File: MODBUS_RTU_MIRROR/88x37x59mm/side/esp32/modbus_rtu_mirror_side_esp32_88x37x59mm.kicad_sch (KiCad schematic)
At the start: 38 parts, among them J1 Conn_01x04_Male, J2 Conn_01x04_Male, J3 Conn_01x06_Male, SW1 SW_Push, U1 ESP32-WROOM-32, U2 TXS0108EPW, U3 AMS1117-3.3, U4 DS3231MZ, U5 FM24C64C

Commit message: created 90 degree 3mm led socket holder
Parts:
- D1: footprint LED_THT:LED_D3.0mm -> LED_THT_horizontal_holder:LED_D3.0mm_4.5x9.5mm
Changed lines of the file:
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@@
     (property "Reference" "D1" (id 0) (at 237.1725 31.75 0))
     (property "Value" "LED" (id 1) (at 237.1725 34.29 0))
-    (property "Footprint" "LED_THT:LED_D3.0mm" (id 2) (at 238.76 38.1 0)
+    (property "Footprint" "LED_THT_horizontal_holder:LED_D3.0mm_4.5x9.5mm" (id 2) (at 238.76 38.1 0)
       (effects (font (size 1.27 1.27)) hide)
     )
@@
     )
     (path "/dc7af683-2c85-4d4e-8d40-70498e51a028"
-      (reference "D1") (unit 1) (value "LED") (footprint "LED_THT:LED_D3.0mm")
+      (reference "D1") (unit 1) (value "LED") (footprint "LED_THT_horizontal_holder:LED_D3.0mm_4.5x9.5mm")
     )
     (path "/5f47507c-41a1-4dac-9fb1-1387dec1beee"

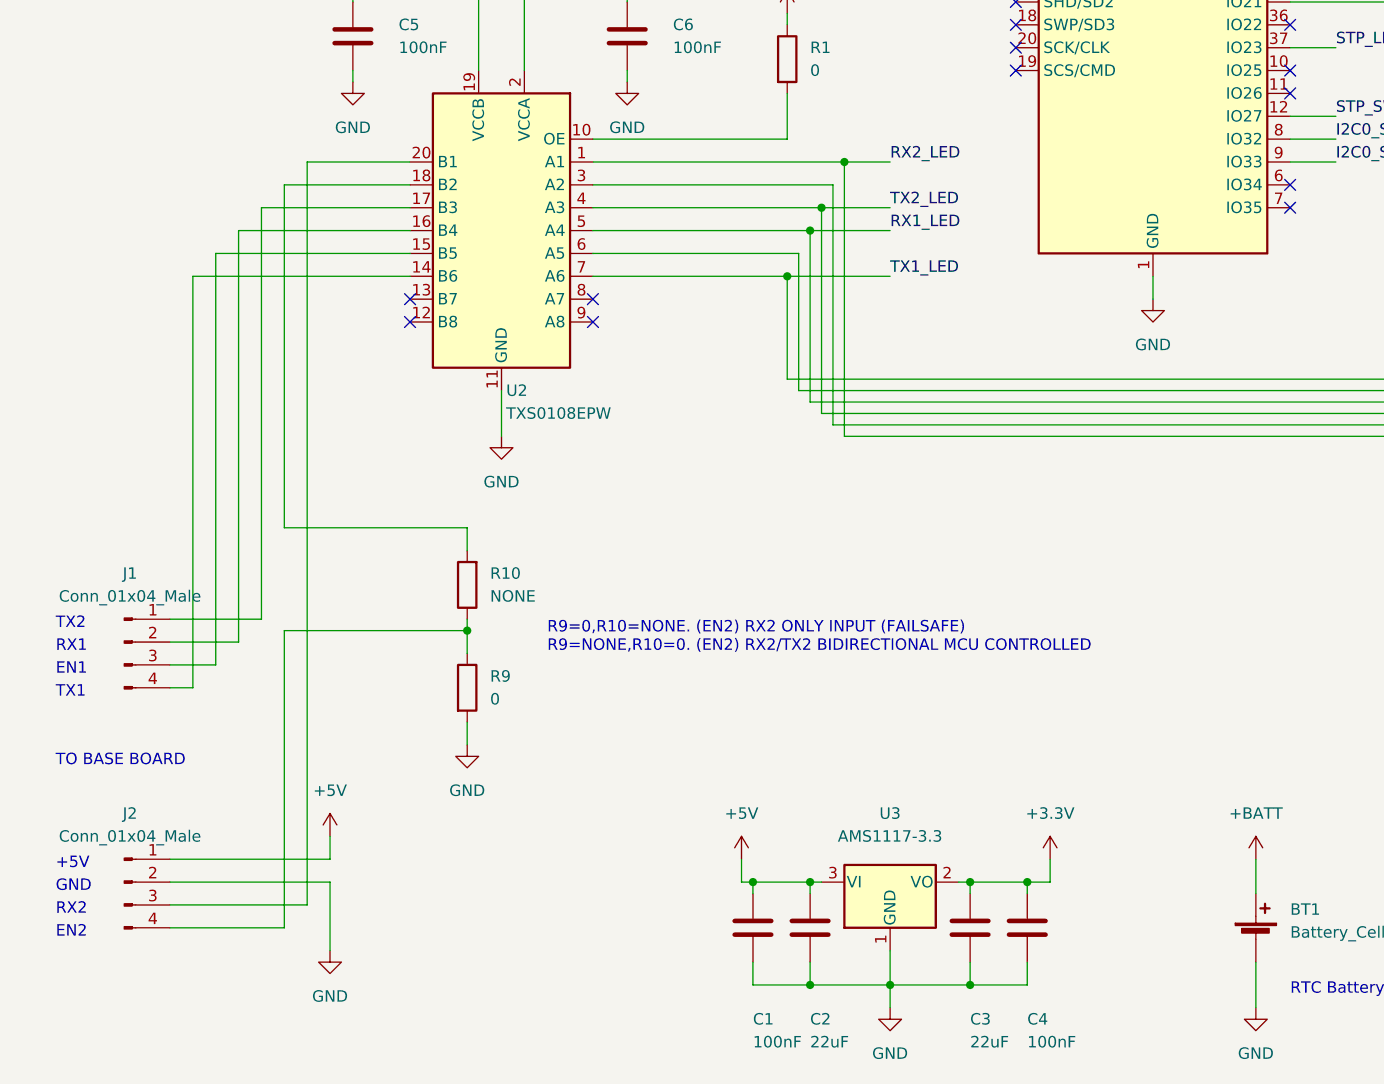
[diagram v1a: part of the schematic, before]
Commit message: changed leds to horizontal and fixed TX1/RX1 disable/enable resistor
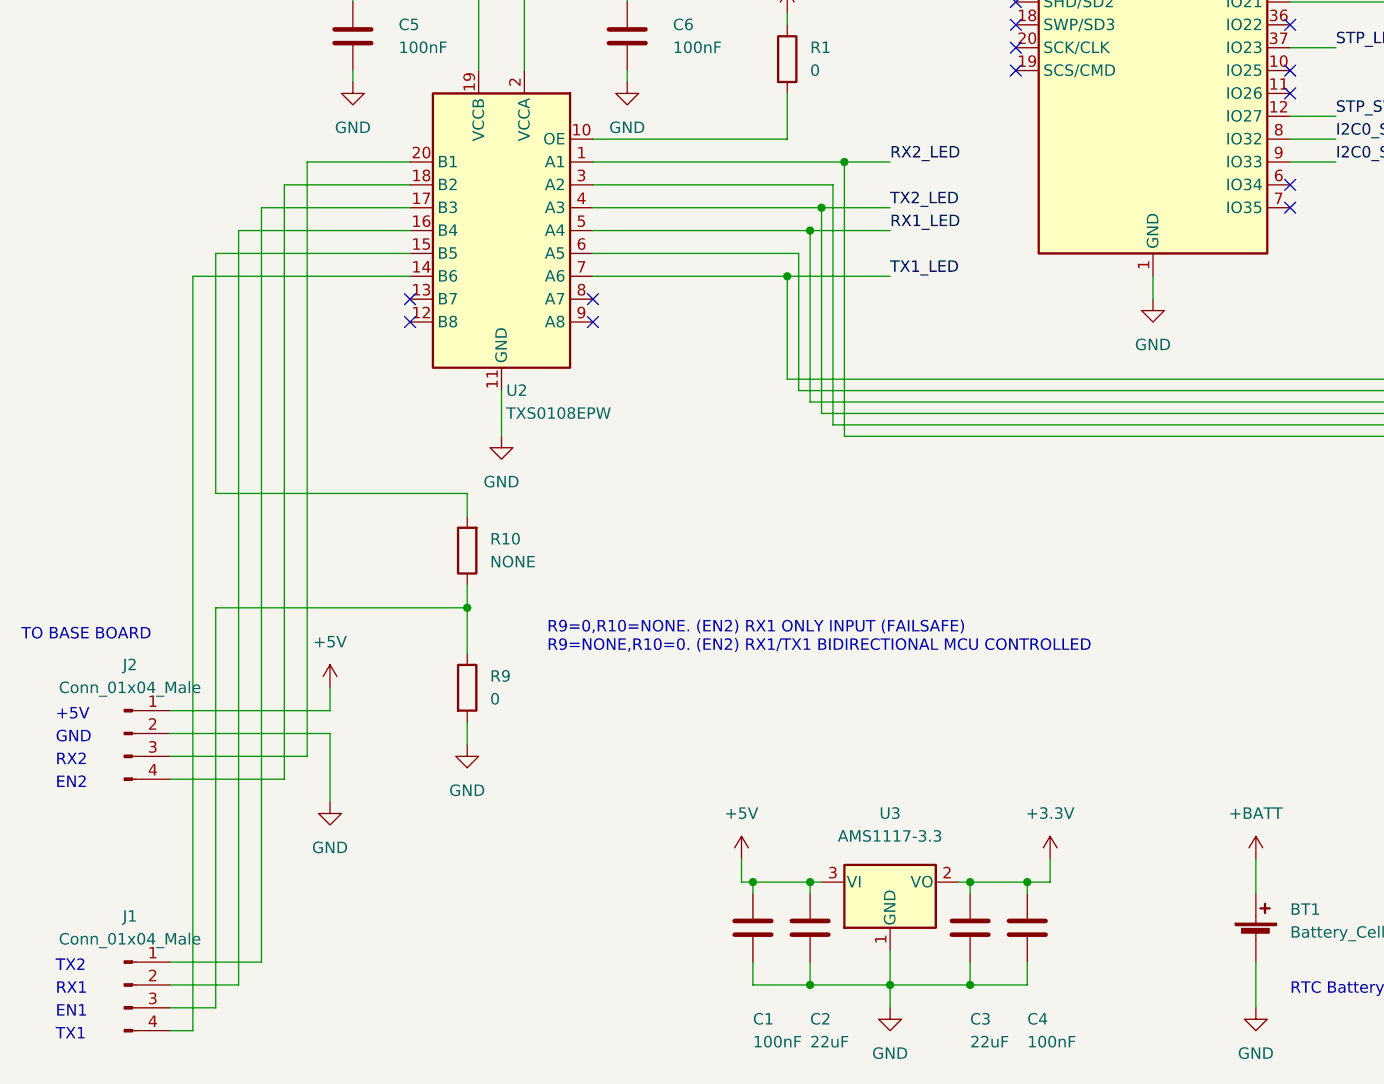
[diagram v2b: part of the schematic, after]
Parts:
- D2, D3, D4, D5, D6: footprint LED_THT:LED_D3.0mm -> LED_THT_horizontal_holder:LED_D3.0mm_4.5x9.5mm
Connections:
- net at J1.3 (Pin_3): now also R10.1, R9.1; no longer U2.15 (B5)
- net at R10.2: now also U2.15 (B5); no longer U2.18 (B2)
- new net: J2.4 (Pin_4), U2.18 (B2)
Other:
- note added: "R9=0,R10=NONE. (EN2) RX1 ONLY INPUT (FAILSAFE) R9=NONE,R10=0. (EN2) RX1/TX1 BIDIRECTIONAL MCU CONTROLLED"
- note removed: "R9=0,R10=NONE. (EN2) RX2 ONLY INPUT (FAILSAFE) R9=NONE,R10=0. (EN2) RX2/TX2 BIDIRECTIONAL MCU CONTROLLED"
- moved on the sheet: J1, J2, R10

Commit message: minor modiffications
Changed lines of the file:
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@@
   (title_block
     (title "Modbus RTU mirror side board")
+    (rev "V2")
   )
   (junction (at 223.52 139.7) (diameter 0) (color 0 0 0 0)
@@
   (no_connect (at 156.21 62.23))
   (no_connect (at 58.42 107.95))
-  (no_connect (at 156.21 57.15))
   (no_connect (at 125.73 69.85))
   (no_connect (at 266.7 137.16))
   (no_connect (at 78.74 110.49))
+  (no_connect (at 156.21 77.47))
   (no_connect (at 125.73 72.39))
   (no_connect (at 156.21 52.07))
@@
   (no_connect (at 156.21 95.25))
   (no_connect (at 125.73 44.45))
+  (no_connect (at 156.21 57.15))
   (no_connect (at 156.21 54.61))
   (no_connect (at 125.73 46.99))
-  (no_connect (at 156.21 77.47))
   (no_connect (at 156.21 97.79))
   (no_connect (at 156.21 44.45))
@@
     (stroke (width 0) (type default) (color 0 0 0 0))
   )
-  (wire (pts (xy 177.8 72.39) (xy 177.8 118.11))
+  (wire (pts (xy 189.23 72.39) (xy 189.23 118.11))
     (stroke (width 0) (type default) (color 0 0 0 0))
   )
@@
     (stroke (width 0) (type default) (color 0 0 0 0))
   )
-  (wire (pts (xy 101.6 118.11) (xy 177.8 118.11))
+  (wire (pts (xy 101.6 118.11) (xy 189.23 118.11))
     (stroke (width 0) (type default) (color 0 0 0 0))
   )
@@
     (stroke (width 0) (type default) (color 0 0 0 0))
   )
-  (wire (pts (xy 156.21 74.93) (xy 176.53 74.93))
+  (wire (pts (xy 156.21 74.93) (xy 187.96 74.93))
     (stroke (width 0) (type default) (color 0 0 0 0))
   )
@@
     (stroke (width 0) (type default) (color 0 0 0 0))
   )
-  (wire (pts (xy 105.41 121.92) (xy 181.61 121.92))
+  (wire (pts (xy 105.41 121.92) (xy 193.04 121.92))
     (stroke (width 0) (type default) (color 0 0 0 0))
   )
@@
     (stroke (width 0) (type default) (color 0 0 0 0))
   )
-  (wire (pts (xy 176.53 116.84) (xy 100.33 116.84))
+  (wire (pts (xy 187.96 116.84) (xy 100.33 116.84))
     (stroke (width 0) (type default) (color 0 0 0 0))
   )
@@
     (stroke (width 0) (type default) (color 0 0 0 0))
   )
-  (wire (pts (xy 180.34 120.65) (xy 104.14 120.65))
+  (wire (pts (xy 191.77 120.65) (xy 104.14 120.65))
     (stroke (width 0) (type default) (color 0 0 0 0))
   )
@@
     (stroke (width 0) (type default) (color 0 0 0 0))
   )
-  (wire (pts (xy 179.07 119.38) (xy 102.87 119.38))
+  (wire (pts (xy 190.5 119.38) (xy 102.87 119.38))
     (stroke (width 0) (type default) (color 0 0 0 0))
   )
@@
     (stroke (width 0) (type default) (color 0 0 0 0))
   )
-  (wire (pts (xy 156.21 49.53) (xy 182.88 49.53))
-    (stroke (width 0) (type default) (color 0 0 0 0))
-  )
-  (wire (pts (xy 176.53 74.93) (xy 176.53 116.84))
+  (wire (pts (xy 156.21 49.53) (xy 194.31 49.53))
+    (stroke (width 0) (type default) (color 0 0 0 0))
+  )
+  (wire (pts (xy 187.96 74.93) (xy 187.96 116.84))
     (stroke (width 0) (type default) (color 0 0 0 0))
   )
@@
     (stroke (width 0) (type default) (color 0 0 0 0))
   )
-  (wire (pts (xy 182.88 123.19) (xy 106.68 123.19))
-    (stroke (width 0) (type default) (color 0 0 0 0))
-  )
-  (wire (pts (xy 156.21 64.77) (xy 181.61 64.77))
+  (wire (pts (xy 194.31 123.19) (xy 106.68 123.19))
+    (stroke (width 0) (type default) (color 0 0 0 0))
+  )
+  (wire (pts (xy 156.21 64.77) (xy 193.04 64.77))
     (stroke (width 0) (type default) (color 0 0 0 0))
   )
@@
     (stroke (width 0) (type default) (color 0 0 0 0))
   )
-  (wire (pts (xy 179.07 69.85) (xy 179.07 119.38))
+  (wire (pts (xy 190.5 69.85) (xy 190.5 119.38))
     (stroke (width 0) (type default) (color 0 0 0 0))
   )
@@
     (stroke (width 0) (type default) (color 0 0 0 0))
   )
-  (wire (pts (xy 180.34 67.31) (xy 180.34 120.65))
+  (wire (pts (xy 191.77 67.31) (xy 191.77 120.65))
     (stroke (width 0) (type default) (color 0 0 0 0))
   )
@@
     (stroke (width 0) (type default) (color 0 0 0 0))
   )
-  (wire (pts (xy 156.21 67.31) (xy 180.34 67.31))
+  (wire (pts (xy 156.21 67.31) (xy 191.77 67.31))
     (stroke (width 0) (type default) (color 0 0 0 0))
   )
@@
     (stroke (width 0) (type default) (color 0 0 0 0))
   )
-  (wire (pts (xy 156.21 69.85) (xy 179.07 69.85))
+  (wire (pts (xy 156.21 69.85) (xy 190.5 69.85))
     (stroke (width 0) (type default) (color 0 0 0 0))
   )
@@
     (stroke (width 0) (type default) (color 0 0 0 0))
   )
-  (wire (pts (xy 156.21 72.39) (xy 177.8 72.39))
+  (wire (pts (xy 156.21 72.39) (xy 189.23 72.39))
     (stroke (width 0) (type default) (color 0 0 0 0))
   )
@@
     (stroke (width 0) (type default) (color 0 0 0 0))
   )
-  (wire (pts (xy 181.61 64.77) (xy 181.61 121.92))
+  (wire (pts (xy 193.04 64.77) (xy 193.04 121.92))
     (stroke (width 0) (type default) (color 0 0 0 0))
   )
@@
     (stroke (width 0) (type default) (color 0 0 0 0))
   )
-  (wire (pts (xy 182.88 49.53) (xy 182.88 123.19))
-    (stroke (width 0) (type default) (color 0 0 0 0))
-  )
+  (wire (pts (xy 194.31 49.53) (xy 194.31 123.19))
+    (stroke (width 0) (type default) (color 0 0 0 0))
+  )

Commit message: started new branch test, with expansion header
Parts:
- added J4, J5: Conn_01x07_Male, Connector_PinHeader_1.00mm:PinHeader_1x07_P1.00mm_Vertical, symbol Connector:Conn_01x07_Male
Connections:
- net STP_LED: now also U1.14 (IO12); no longer U1.37 (IO23)
- net STP_SW: now also U1.7 (IO35); no longer U1.12 (IO27)
- net ESP_IO36: now reaches U1.4 (SENSOR_VP)
- net ESP_IO36: now also J4.4 (Pin_4)
- net ESP_IO39: now reaches U1.5 (SENSOR_VN)
- net ESP_IO39: now also J4.3 (Pin_3)
- net ESP_IO34: now reaches U1.6 (IO34)
- net ESP_IO34: now also J4.2 (Pin_2)
- new net ESP_IO23: J4.5 (Pin_5), U1.37 (IO23)
- new net ESP_IO27: J4.1 (Pin_1), U1.12 (IO27)
- no-connect marks 26 -> 30
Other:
- moved on the sheet: D1, D2, D3, D4, D5, D6, R2, R3, R4, R5, R6, R7

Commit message: expansion connector routed
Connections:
- net +3.3V: now also J5.2 (Pin_2)
- net +5V: now also J5.1 (Pin_1)
- net ESP_IO23: now also J4.7 (Pin_7); no longer J4.5 (Pin_5)
- net ESP_IO27: now also J4.3 (Pin_3); no longer J4.1 (Pin_1)
- net ESP_IO34: now also J4.4 (Pin_4); no longer J4.2 (Pin_2)
- net ESP_IO36: now also J4.6 (Pin_6); no longer J4.4 (Pin_4)
- net ESP_IO39: now also J4.5 (Pin_5); no longer J4.3 (Pin_3)
- net GND: now also J5.3 (Pin_3), J5.4 (Pin_4)
- net ESP_IO26: now reaches J5.5 (Pin_5)
- net ESP_IO26: now also U1.11 (IO26)
- net ESP_IO25: now reaches J5.6 (Pin_6)
- net ESP_IO25: now also U1.10 (IO25)
- net ESP_IO22: now reaches J5.7 (Pin_7)
- net ESP_IO22: now also U1.36 (IO22)
- net ESP_IO14: now reaches U1.13 (IO14)
- net ESP_IO14: now also J4.1 (Pin_1)
- net ESP_IO13: now reaches U1.16 (IO13)
- net ESP_IO13: now also J4.2 (Pin_2)
- no-connect marks 30 -> 16
